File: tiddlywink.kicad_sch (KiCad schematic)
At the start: 78 parts

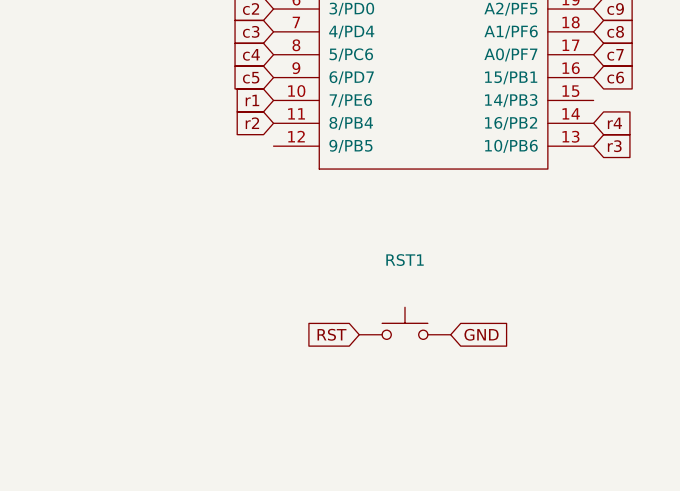
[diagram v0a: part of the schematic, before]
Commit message: minor pcb updates
added silk to front
moved reset button position
adjusted a few traces
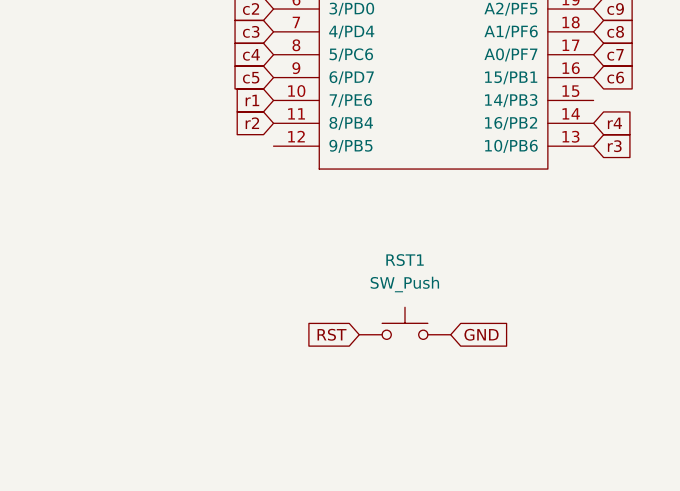
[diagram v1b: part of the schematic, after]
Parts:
- RST1: value (none) -> SW_Push; footprint (none) -> Keebio-Parts:SW_SPST_TL3342
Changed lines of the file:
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@@
     (in_bom yes) (on_board yes) (fields_autoplaced)
     (property "Reference" "RST1" (id 0) (at 177.165 66.04 0))
-    (property "Value" "" (id 1) (at 177.165 68.58 0))
-    (property "Footprint" "" (id 2) (at 177.165 69.215 0)
+    (property "Value" "SW_Push" (id 1) (at 177.165 68.58 0))
+    (property "Footprint" "Keebio-Parts:SW_SPST_TL3342" (id 2) (at 177.165 69.215 0)
       (effects (font (size 1.27 1.27)) hide)
     )

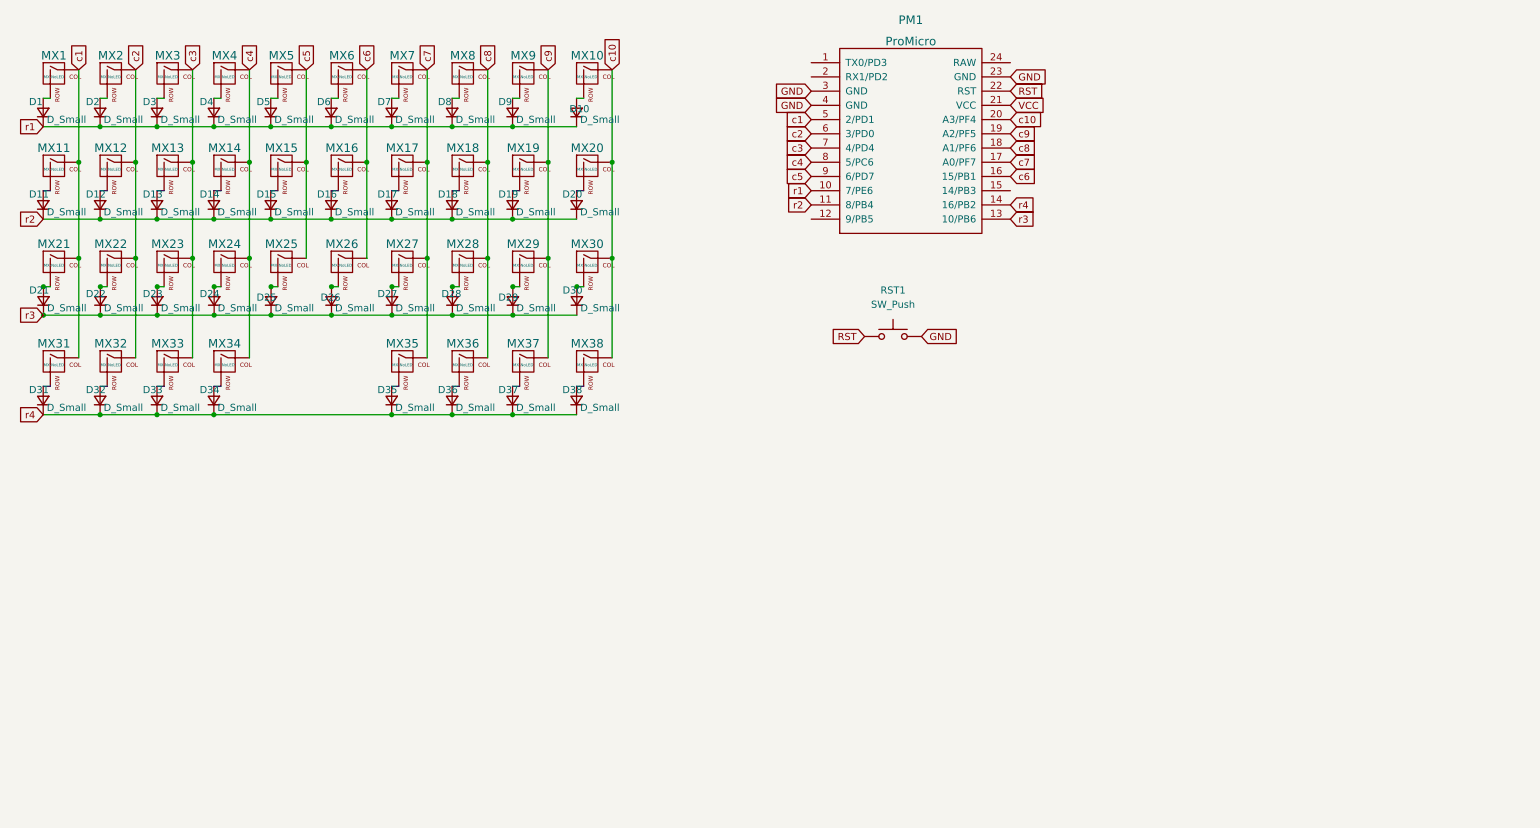
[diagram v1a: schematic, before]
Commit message: big update
added rgb support
updated case files
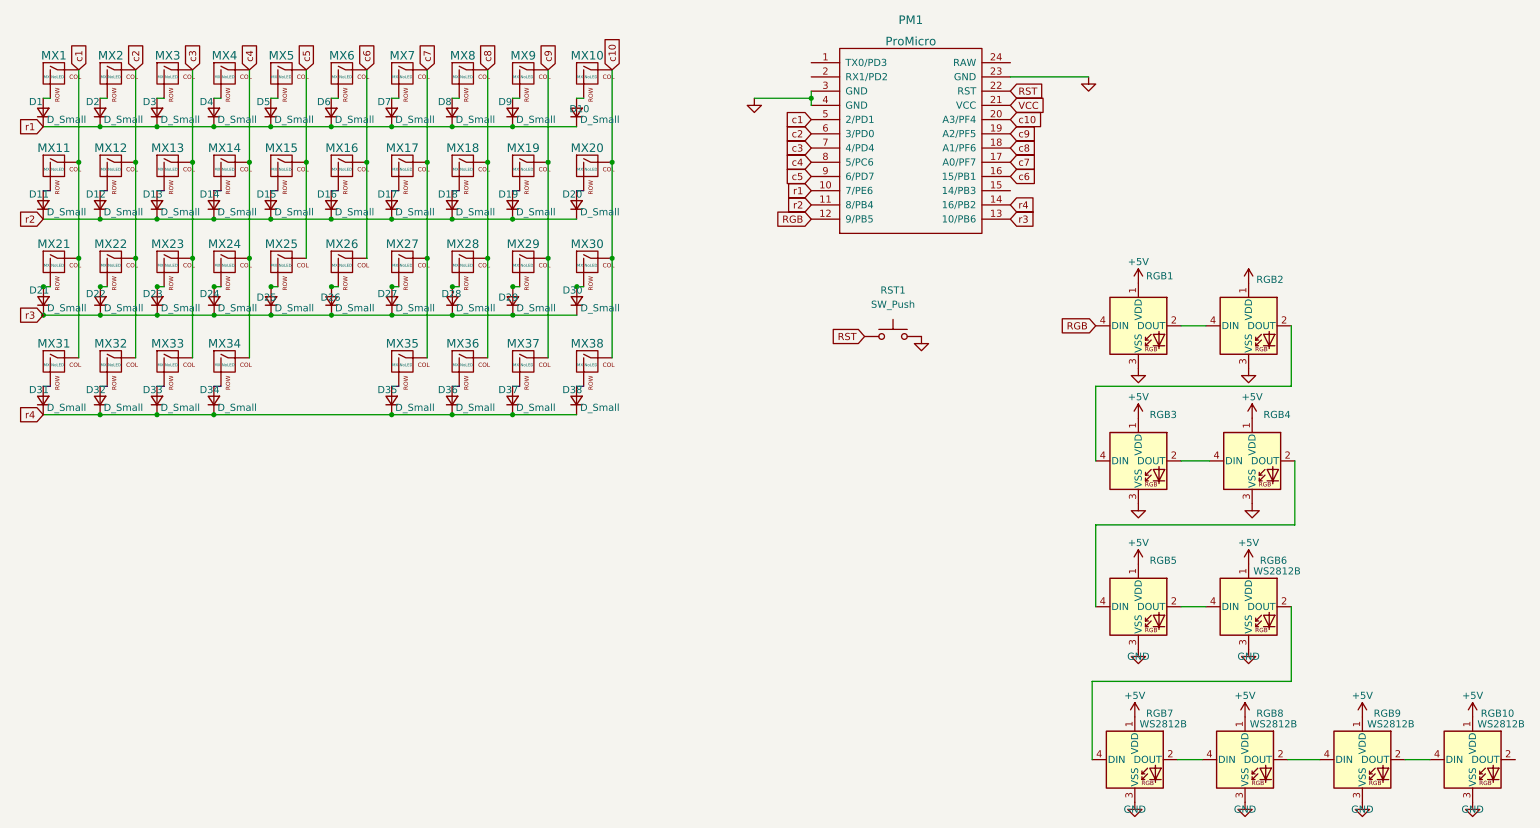
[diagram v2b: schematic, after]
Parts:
- added RGB1, RGB2, RGB3, RGB4, RGB5: (no value), symbol LED:WS2812B
- added RGB10, RGB6, RGB7, RGB8, RGB9: WS2812B, LED_SMD:LED_WS2812B_PLCC4_5.0x5.0mm_P3.2mm, symbol LED:WS2812B
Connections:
- net GND: now also RGB1.3 (VSS), RGB10.3 (VSS), RGB2.3 (VSS), RGB3.3 (VSS), RGB4.3 (VSS), RGB5.3 (VSS), RGB6.3 (VSS), RGB7.3 (VSS), RGB8.3 (VSS), RGB9.3 (VSS)
- net RGB: now reaches PM1.12 (9/PB5)
- net RGB: now also RGB1.4 (DIN)
- new net: RGB2.2 (DOUT), RGB3.4 (DIN)
- new net: RGB1.2 (DOUT), RGB2.4 (DIN)
- new net: RGB10.4 (DIN), RGB9.2 (DOUT)
- new net: RGB8.2 (DOUT), RGB9.4 (DIN)
- new net: RGB3.2 (DOUT), RGB4.4 (DIN)
- new net: RGB6.2 (DOUT), RGB7.4 (DIN)
- new net: RGB5.2 (DOUT), RGB6.4 (DIN)
- new net: RGB7.2 (DOUT), RGB8.4 (DIN)
- new net: RGB4.2 (DOUT), RGB5.4 (DIN)
- new net +5V: RGB1.1 (VDD), RGB10.1 (VDD), RGB2.1 (VDD), RGB3.1 (VDD), RGB4.1 (VDD), RGB5.1 (VDD), RGB6.1 (VDD), RGB7.1 (VDD), RGB8.1 (VDD), RGB9.1 (VDD)

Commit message: Rotary Encoder Support
added rotary encoder support on B and second B
moved some diodes
updated traces to match
updated gerber files
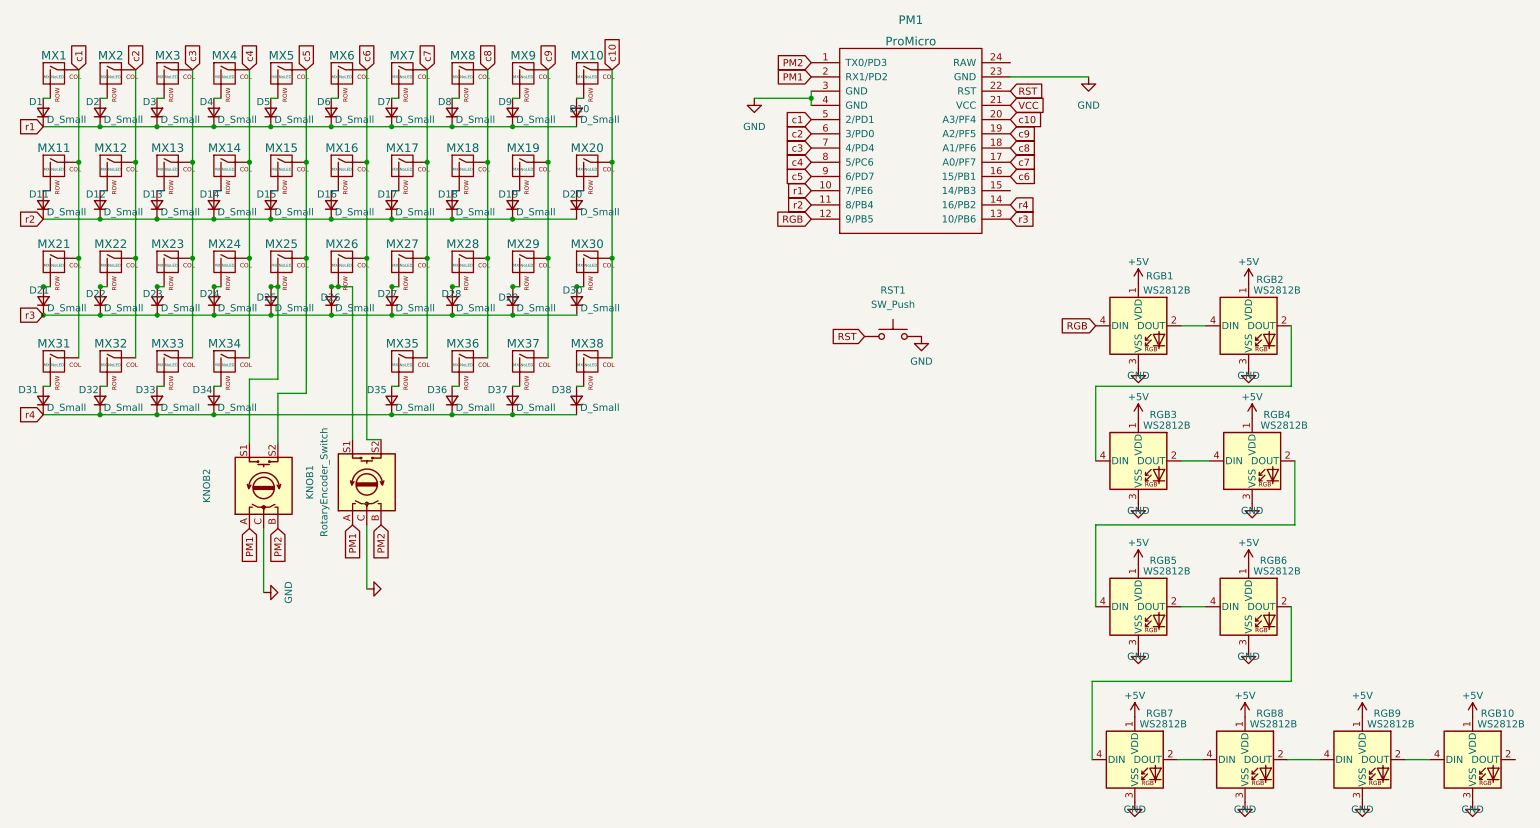
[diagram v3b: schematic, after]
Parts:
- added KNOB1: RotaryEncoder_Switch, Rotary_Encoder:RotaryEncoder_Alps_EC11E-Switch_Vertical_H20mm_CircularMountingHoles, symbol Device:RotaryEncoder_Switch
- added KNOB2: (no value), symbol Device:RotaryEncoder_Switch
- RGB1, RGB2, RGB3, RGB4, RGB5: value (none) -> WS2812B; footprint (none) -> LED_SMD:LED_WS2812B_PLCC4_5.0x5.0mm_P3.2mm
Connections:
- net GND: now also KNOB1.C, KNOB2.C
- net c5: now also KNOB2.S2
- net c6: now also KNOB1.S2
- net at D26.2 (A), MX26.2 (ROW): now also KNOB1.S1
- net at MX33.2 (ROW): now also D33.2 (A)
- net at D25.2 (A), MX25.2 (ROW): now also KNOB2.S1
- net at MX36.2 (ROW): now also D36.2 (A)
- net at MX35.2 (ROW): now also D35.2 (A)
- net at MX31.2 (ROW): now also D31.2 (A)
- net at MX38.2 (ROW): now also D38.2 (A)
- net at D37.2 (A): now also MX37.2 (ROW)
- net PM2: now reaches PM1.1 (TX0/PD3)
- net PM2: now also KNOB1.B, KNOB2.B
- net PM1: now reaches PM1.2 (RX1/PD2)
- net PM1: now also KNOB1.A, KNOB2.A
- net at MX34.2 (ROW): now also D34.2 (A)
- net at D32.2 (A): now also MX32.2 (ROW)

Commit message: fix rgb
uses vcc symbol in schematic
connects vcc from pro micro to rgbs
connects disconnected gnd fill with vias
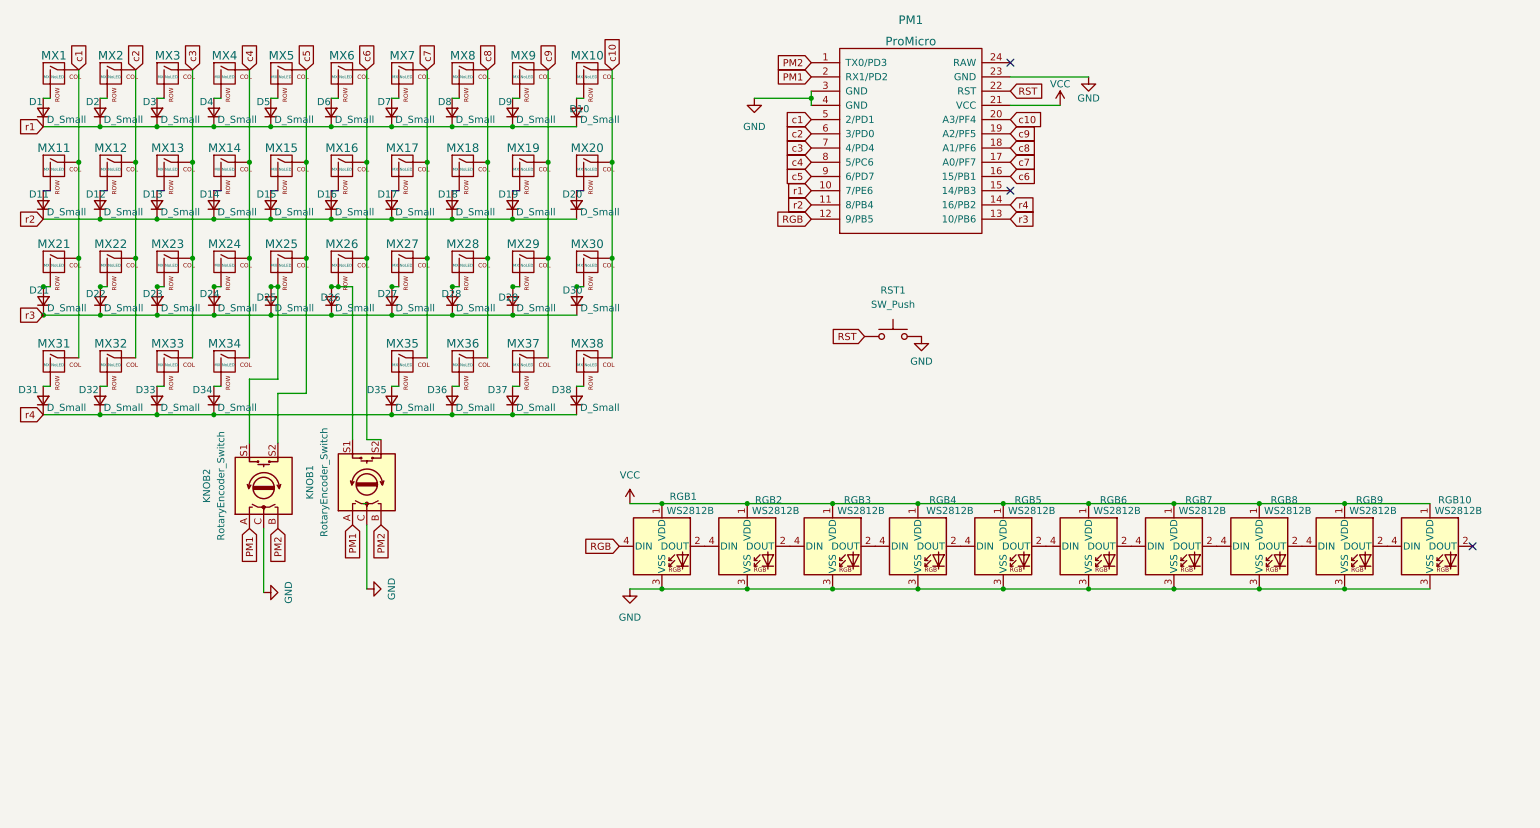
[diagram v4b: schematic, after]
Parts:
- KNOB2: value (none) -> RotaryEncoder_Switch; footprint (none) -> Rotary_Encoder:RotaryEncoder_Alps_EC11E-Switch_Vertical_H20mm_CircularMountingHoles
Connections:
- net +5V is gone; now on net VCC: RGB1.1 (VDD), RGB10.1 (VDD), RGB2.1 (VDD), RGB3.1 (VDD), RGB4.1 (VDD), RGB5.1 (VDD), RGB6.1 (VDD), RGB7.1 (VDD), RGB8.1 (VDD), RGB9.1 (VDD)
- no-connect marks 0 -> 3
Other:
- title: (none) -> Tiddlywink
- moved on the sheet: RGB1, RGB10, RGB2, RGB3, RGB4, RGB5, RGB6, RGB7, RGB8, RGB9
